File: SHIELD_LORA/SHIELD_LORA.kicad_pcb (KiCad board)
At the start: 2 copper layers, 2 parts

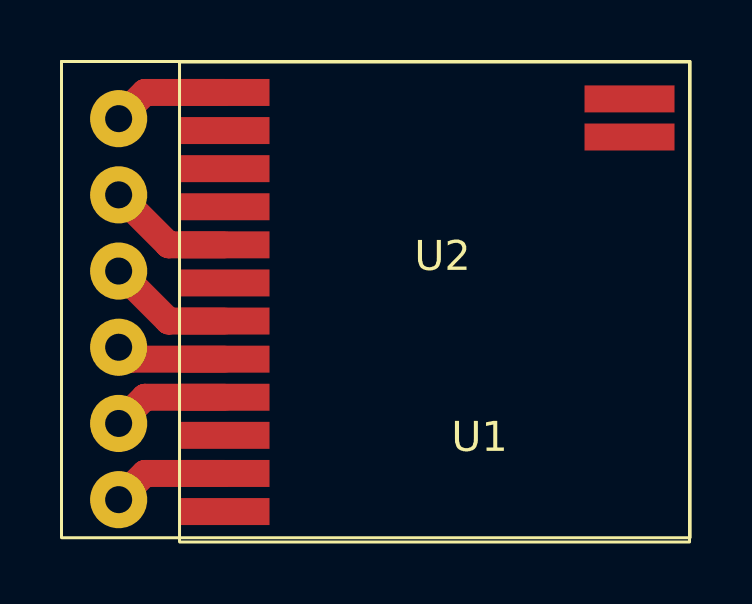
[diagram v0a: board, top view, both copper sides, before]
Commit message: esquematico finalizado, PCB en proceso.
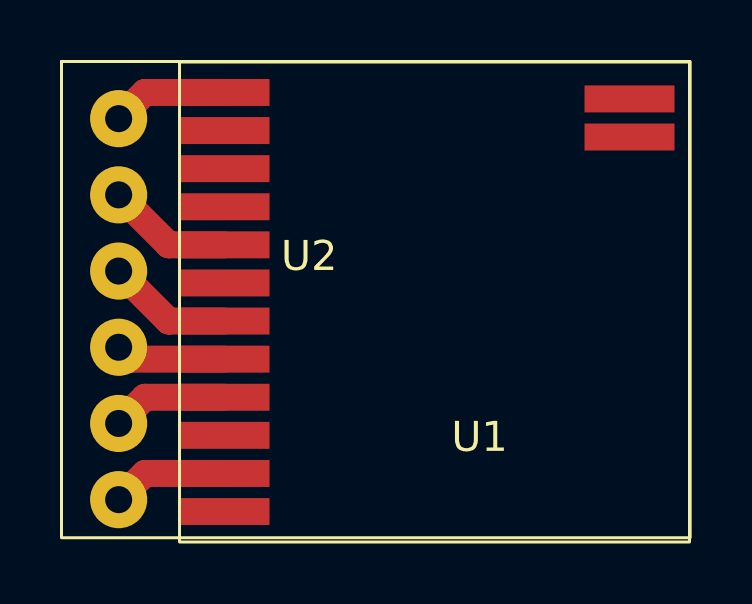
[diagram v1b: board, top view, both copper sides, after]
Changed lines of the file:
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@@
 		(at 159.755 91.59)
 		(property "Reference" "U2"
-			(at -8.255 9.025 0)
+			(at -12.7 9.025 0)
 			(unlocked yes)
 			(layer "F.SilkS")
@@
 		)
 		(property "Value" "~"
-			(at -8.255 10.525 0)
+			(at -12.7 10.525 0)
 			(unlocked yes)
 			(layer "F.Fab")
@@
 		)
 		(fp_text user "${REFERENCE}"
-			(at -8.255 12.025 0)
+			(at -12.7 12.025 0)
 			(unlocked yes)
 			(layer "F.Fab")
@@
 		)
 		(fp_text user "${REFERENCE}"
-			(at -7 17.915 0)
+			(at -13.955 17.915 0)
 			(unlocked yes)
 			(layer "F.Fab")
@@
 	)
 	(segment
+		(start 141.578 107.862)
+		(end 144.234 107.862)
+		(width 0.9)
+		(layer "F.Cu")
+		(net 2)
+	)
+	(segment
 		(start 140.705 108.735)
 		(end 141.578 107.862)
@@
 	)
 	(segment
-		(start 141.578 107.862)
-		(end 144.234 107.862)
-		(width 0.9)
-		(layer "F.Cu")
-		(net 2)
+		(start 140.705 96.035)
+		(end 141.578 95.162)
+		(width 0.9)
+		(layer "F.Cu")
+		(net 4)
 	)
 	(segment
@@
 	)
 	(segment
-		(start 140.705 96.035)
-		(end 141.578 95.162)
-		(width 0.9)
-		(layer "F.Cu")
-		(net 4)
+		(start 142.372 100.242)
+		(end 144.234 100.242)
+		(width 0.9)
+		(layer "F.Cu")
+		(net 6)
 	)
 	(segment
@@
 	)
 	(segment
-		(start 142.372 100.242)
-		(end 144.234 100.242)
-		(width 0.9)
-		(layer "F.Cu")
-		(net 6)
+		(start 140.705 103.655)
+		(end 141.102 104.052)
+		(width 0.9)
+		(layer "F.Cu")
+		(net 7)
 	)
 	(segment
@@
 	)
 	(segment
-		(start 140.705 103.655)
-		(end 141.102 104.052)
-		(width 0.9)
-		(layer "F.Cu")
-		(net 7)
+		(start 140.705 106.195)
+		(end 141.578 105.322)
+		(width 0.9)
+		(layer "F.Cu")
+		(net 8)
 	)
 	(segment
@@
 		(width 0.9)
 		(layer "F.Cu")
-		(net 8)
-	)
-	(segment
-		(start 140.705 106.195)
-		(end 141.578 105.322)
-		(width 0.9)
-		(layer "F.Cu")
